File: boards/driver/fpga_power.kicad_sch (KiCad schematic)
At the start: 40 parts, among them J1 Barrel_Jack_Switch, J2 Conn_01x24, J3 Conn_02x06_Top_Bottom, J4 Conn_01x24, Q90 IRF7413, U10 74LVC245, U11 74LVC245, U12 JTE0624D05, U13 LTC4231-1, U14 74HC4514, U15 74LVC2G04, U16 74LVC2G04, U17 74LVC2G04, U18 74LVC2G04

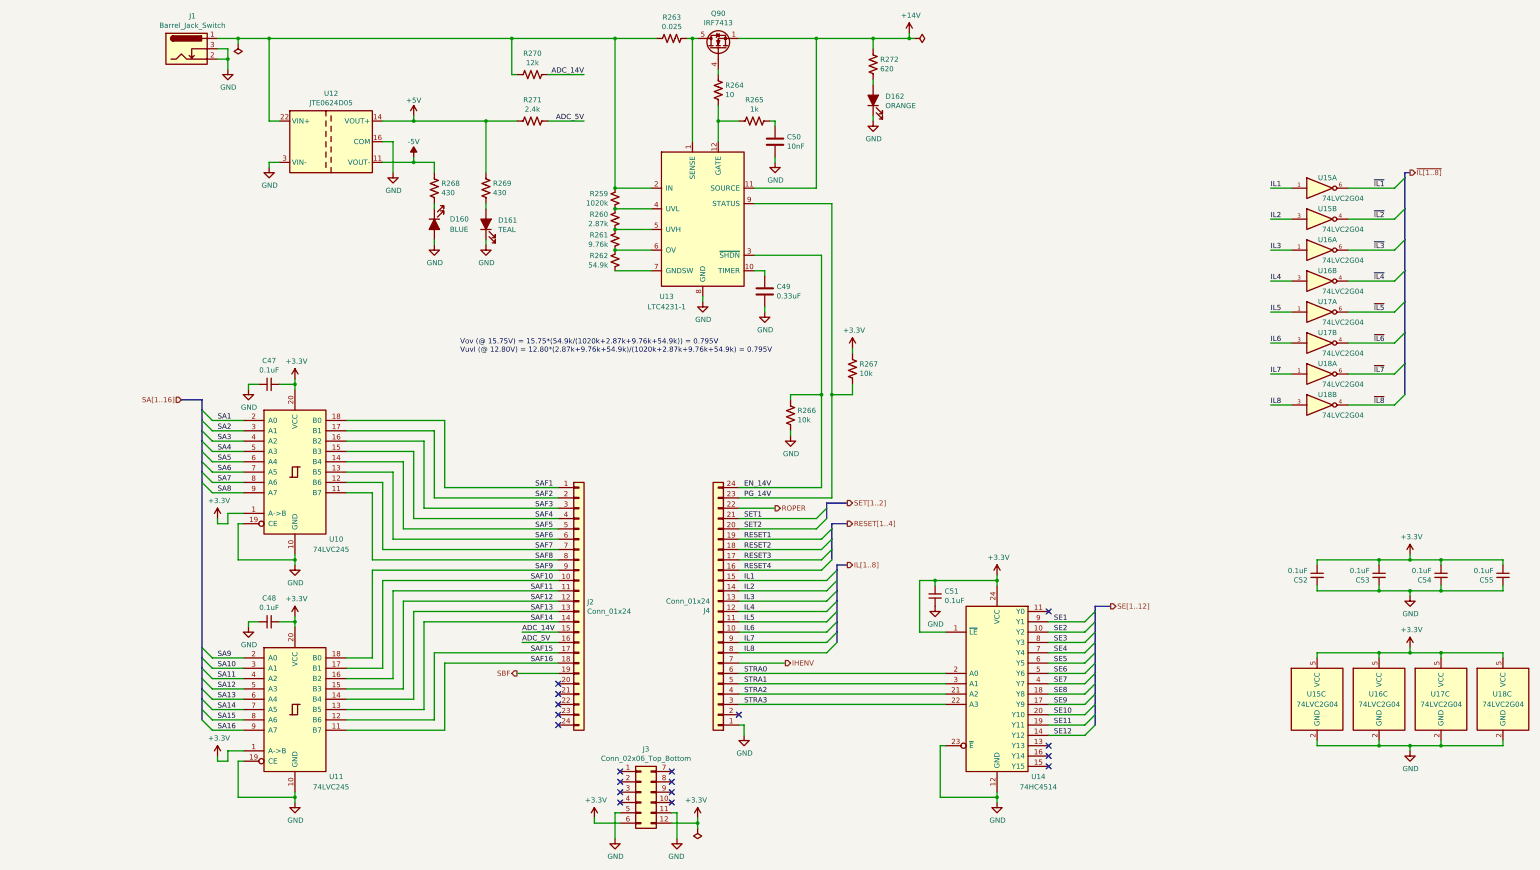
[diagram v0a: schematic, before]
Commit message: Driver: Added a 5V->3.3V LDO to replace the reversed cmod header, added jumpers for the 200R parallel returns, and renamed subcircuit ports to avoid unexpected ground connections.
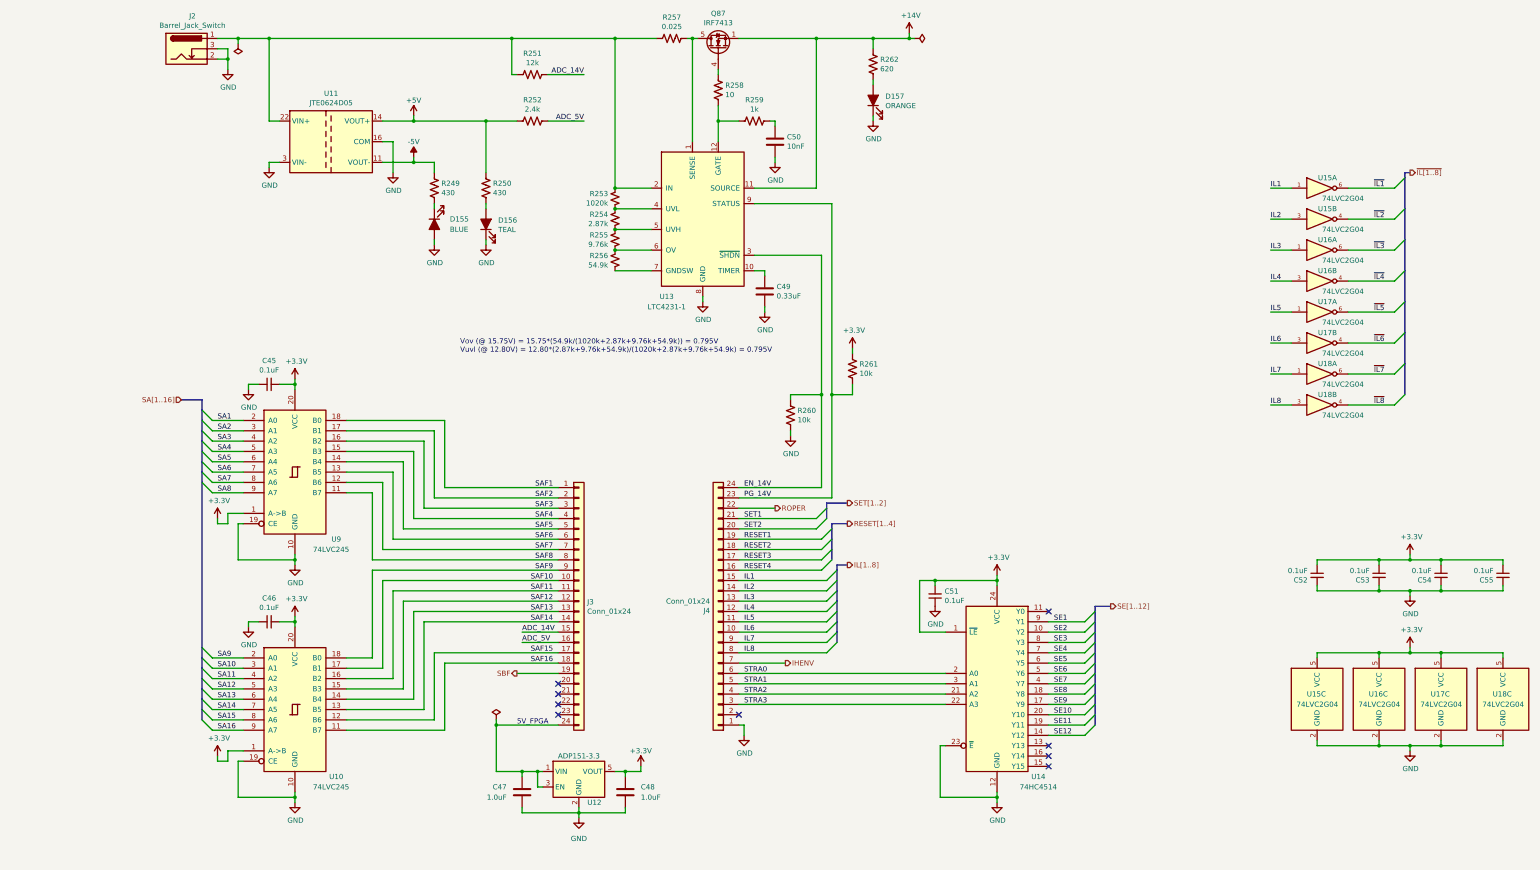
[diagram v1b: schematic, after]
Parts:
- removed J3: Conn_02x06_Top_Bottom, Connector_PinSocket_2.54mm:PinSocket_2x06_P2.54mm_Vertical, symbol Connector_Generic:Conn_02x06_Top_Bottom
- added C47, C48: 1.0uF, symbol Device:C
- added U12: ADP151-3.3, symbol lachesis:ADP151-3.3
- renumbered C47 to C45, C48 to C46, D160 to D155, D161 to D156, D162 to D157, J1 to J2, J2 to J3, Q90 to Q87, R268 to R249, R269 to R250, R270 to R251, R271 to R252, R259 to R253, R260 to R254, R261 to R255, R262 to R256, R263 to R257, R264 to R258, R265 to R259, R266 to R260, R267 to R261, R272 to R262, U11 to U10, U12 to U11, U10 to U9
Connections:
- net +3V3: now also C48.1, U12.5 (VOUT)
- net GND: now also C47.1, C48.2, U12.2 (GND)
- net at J3.24 (Pin_24): now also C47.2, U12.1 (VIN), U12.3 (EN)
- no-connect marks 18 -> 9
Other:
- note added: "5V_FPGA"

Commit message: Driver: incorporated most changes from the test board, and began layout
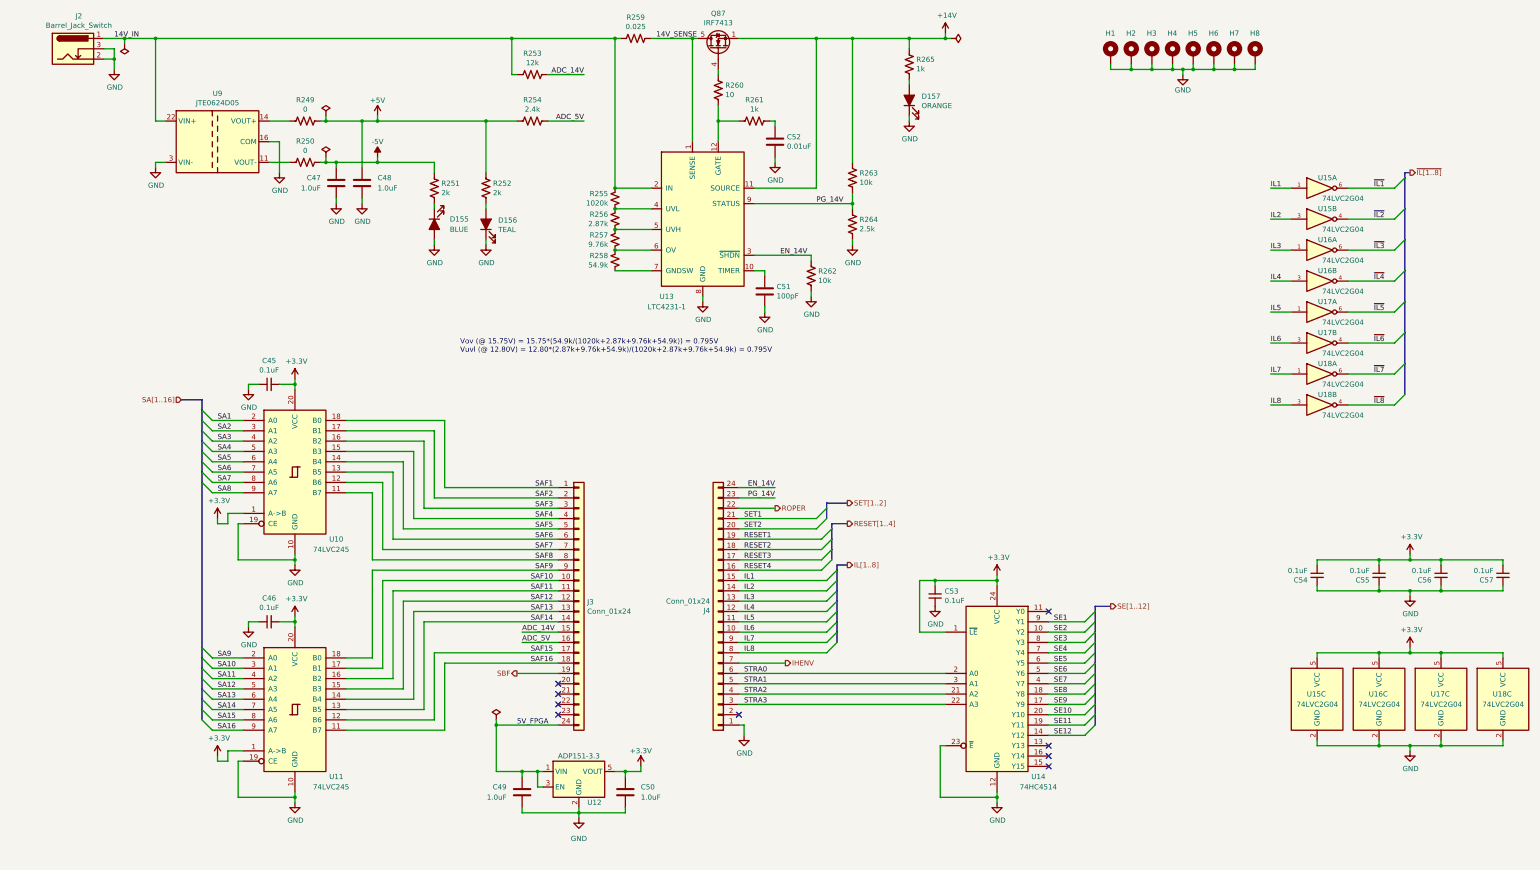
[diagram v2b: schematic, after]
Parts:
- added C47, C48: 1.0uF, Capacitor_SMD:C_0805_2012Metric, symbol Device:C
- added H1, H2, H3, H4, H5, H6, H7, H8: MountingHole_Pad, lachesis:MountingHole_No2_Pad, symbol Mechanical:MountingHole_Pad
- added R249, R250: 0, Resistor_SMD:R_0805_2012Metric, symbol Device:R_US
- added R264: 2.5k, Resistor_SMD:R_0603_1608Metric, symbol Device:R_US
- C49: renamed from C47; footprint (none) -> Capacitor_SMD:C_0603_1608Metric
- C50: renamed from C48; footprint (none) -> Capacitor_SMD:C_0603_1608Metric
- C51: renamed from C49; value 0.33uF -> 100pF
- C52: renamed from C50; value 10nF -> 0.01uF
- R251: renamed from R249; value 430 -> 2k
- R252: renamed from R250; value 430 -> 2k
- R259: renamed from R257; footprint Resistor_SMD:R_0603_1608Metric -> Resistor_SMD:R_1206_3216Metric
- R265: renamed from R262; value 620 -> 1k
- U12: footprint (none) -> Package_TO_SOT_SMD:TSOT-23-5
- renumbered C51 to C53, C52 to C54, C53 to C55, C54 to C56, C55 to C57, R251 to R253, R252 to R254, R253 to R255, R254 to R256, R255 to R257, R256 to R258, R258 to R260, R259 to R261, R260 to R262, R261 to R263, U9 to U10, U10 to U11, U11 to U9
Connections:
- net +14V: now also R263.1
- net +3V3: no longer R263.1
- net +5V: now also C48.1, R249.1; no longer U9.14 (VOUT+)
- net -5V: now also C47.2, R250.1; no longer U9.11 (VOUT-)
- net GND: now also C47.1, C48.2, H1.1, H2.1, H3.1, H4.1, H5.1, H6.1, H7.1, H8.1, R264.2
- net PG_14V: now also R264.1
- net 14V_SENSE: now reaches Q87.5 (D), Q87.6 (D), Q87.7 (D), Q87.8 (D), R259.1, U13.1 (SENSE)
- net 14V_IN: now reaches J2.1, R253.2, R255.2, R259.2, U13.2 (IN), U9.22 (VIN+), U9.23 (VIN+)
- new net: R250.2, U9.11 (VOUT-)
- new net: R249.2, U9.14 (VOUT+)
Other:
- moved on the sheet: D157, J2, R259, R262, R263, R265, U9

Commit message: Driver: lightly reorganized FPGA wiring to make it easier to change in the future, and fixed sense amp mapping
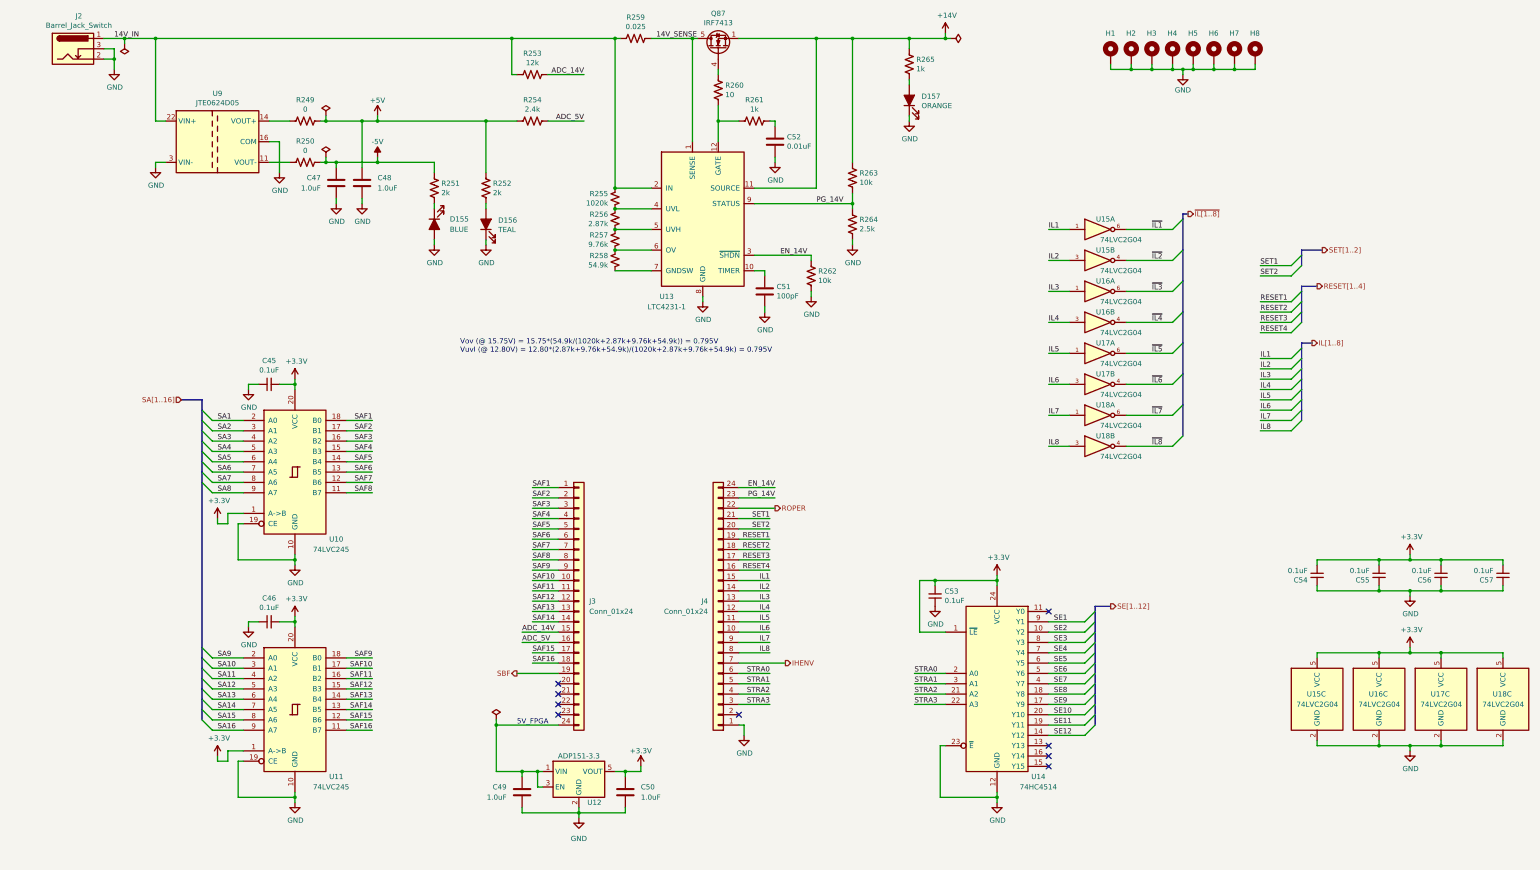
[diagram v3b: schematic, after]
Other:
- moved on the sheet: U15A, U15B, U16A, U16B, U17A, U17B, U18A, U18B

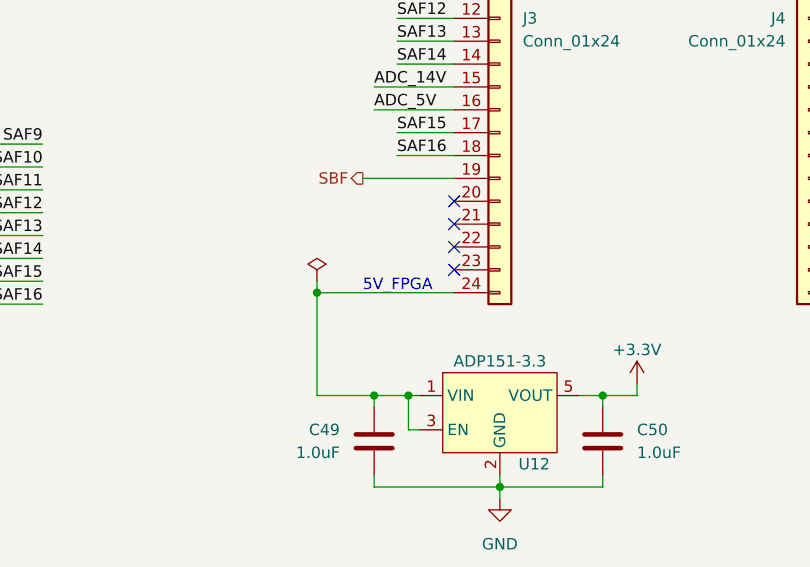
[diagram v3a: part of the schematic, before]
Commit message: Driver: progress on subcircuit layout and overall placement
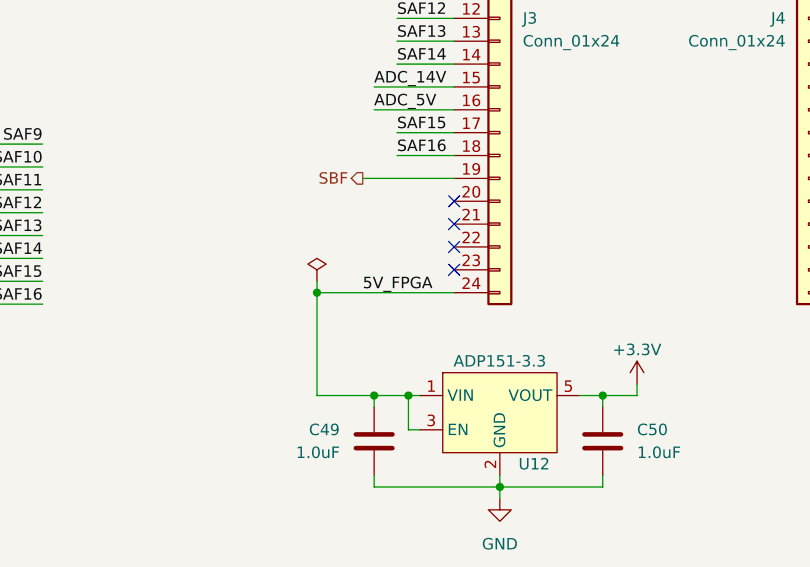
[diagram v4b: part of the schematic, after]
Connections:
- net 5V_FPGA: now reaches C49.2, J3.24 (Pin_24), U12.1 (VIN), U12.3 (EN)
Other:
- note removed: "5V_FPGA"
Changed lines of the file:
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@@
-    (effects (font (size 1.27 1.27)) (justify left bottom))
-  )
-  (text "5V_FPGA" (at 142.24 205.74 0)
     (effects (font (size 1.27 1.27)) (justify left bottom))
   )
@@
     (effects (font (size 1.27 1.27)) (justify left bottom))
   )
+  (label "5V_FPGA" (at 142.24 205.74 0)
+    (effects (font (size 1.27 1.27)) (justify left bottom))
+  )

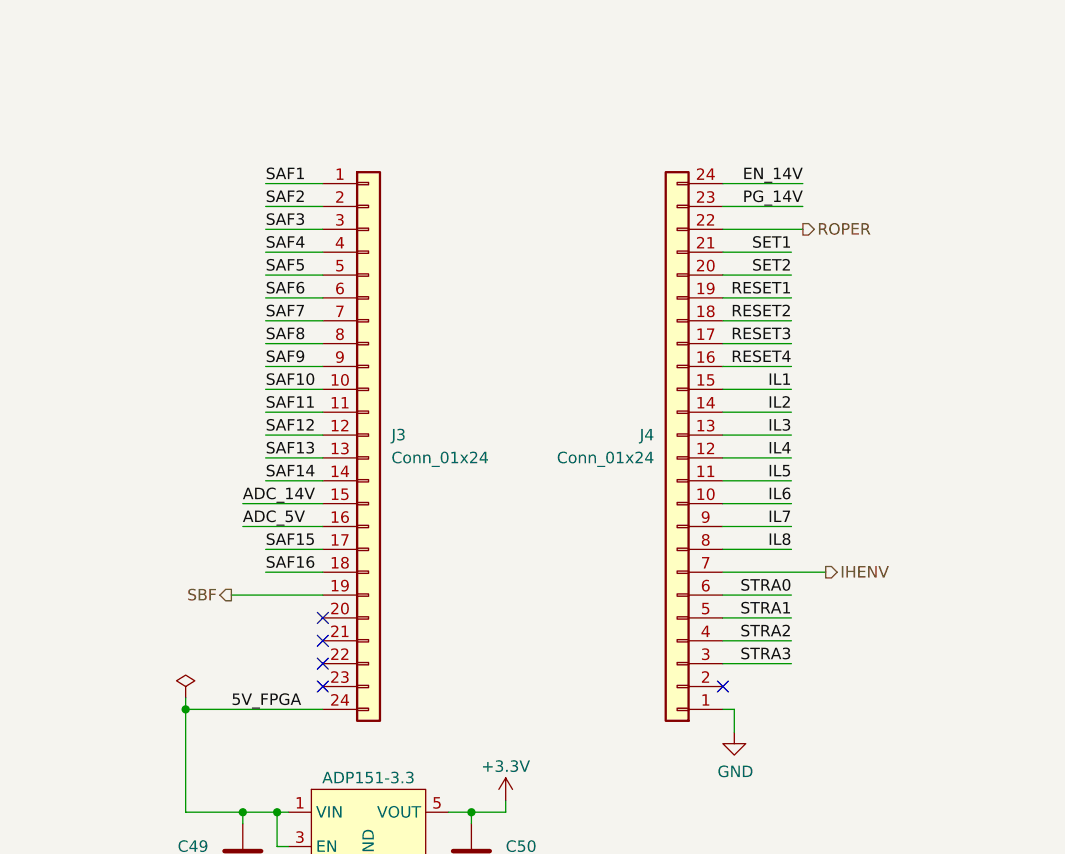
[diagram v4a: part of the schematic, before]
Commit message: Driver: 3.3V section is now laid out, contained entirely beneath the FPGA daughter board
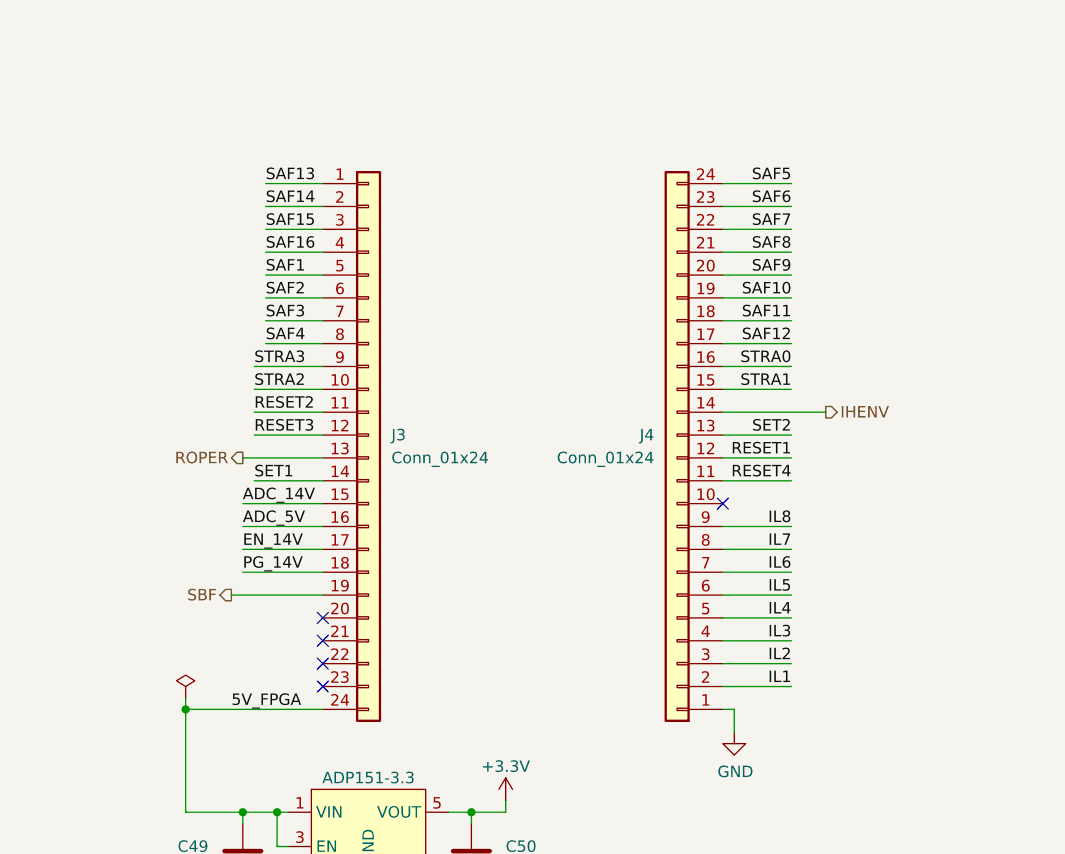
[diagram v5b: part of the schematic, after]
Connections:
- net EN_14V: now also J3.17 (Pin_17); no longer J4.24 (Pin_24)
- net IHENV: now also J4.14 (Pin_14); no longer J4.7 (Pin_7)
- net IL1: now also J4.2 (Pin_2); no longer J4.15 (Pin_15)
- net IL2: now also J4.3 (Pin_3); no longer J4.14 (Pin_14)
- net IL3: now also J4.4 (Pin_4); no longer J4.13 (Pin_13)
- net IL4: now also J4.5 (Pin_5); no longer J4.12 (Pin_12)
- net IL5: now also J4.6 (Pin_6); no longer J4.11 (Pin_11)
- net IL6: now also J4.7 (Pin_7); no longer J4.10 (Pin_10)
- net IL7: now also J4.8 (Pin_8); no longer J4.9 (Pin_9)
- net IL8: now also J4.9 (Pin_9); no longer J4.8 (Pin_8)
- net PG_14V: now also J3.18 (Pin_18); no longer J4.23 (Pin_23)
- net RESET1: now also J4.12 (Pin_12); no longer J4.19 (Pin_19)
- net RESET2: now also J3.11 (Pin_11); no longer J4.18 (Pin_18)
- net RESET3: now also J3.12 (Pin_12); no longer J4.17 (Pin_17)
- net RESET4: now also J4.11 (Pin_11); no longer J4.16 (Pin_16)
- net ROPER: now also J3.13 (Pin_13); no longer J4.22 (Pin_22)
- net SAF1: now also J3.5 (Pin_5); no longer J3.1 (Pin_1)
- net SAF10: now also J4.19 (Pin_19); no longer J3.10 (Pin_10)
- net SAF11: now also J4.18 (Pin_18); no longer J3.11 (Pin_11)
- net SAF12: now also J4.17 (Pin_17); no longer J3.12 (Pin_12)
- net SAF13: now also J3.1 (Pin_1); no longer J3.13 (Pin_13)
- net SAF14: now also J3.2 (Pin_2); no longer J3.14 (Pin_14)
- net SAF15: now also J3.3 (Pin_3); no longer J3.17 (Pin_17)
- net SAF16: now also J3.4 (Pin_4); no longer J3.18 (Pin_18)
- net SAF2: now also J3.6 (Pin_6); no longer J3.2 (Pin_2)
- net SAF3: now also J3.7 (Pin_7); no longer J3.3 (Pin_3)
- net SAF4: now also J3.8 (Pin_8); no longer J3.4 (Pin_4)
- net SAF5: now also J4.24 (Pin_24); no longer J3.5 (Pin_5)
- net SAF6: now also J4.23 (Pin_23); no longer J3.6 (Pin_6)
- net SAF7: now also J4.22 (Pin_22); no longer J3.7 (Pin_7)
- net SAF8: now also J4.21 (Pin_21); no longer J3.8 (Pin_8)
- net SAF9: now also J4.20 (Pin_20); no longer J3.9 (Pin_9)
- net SET1: now also J3.14 (Pin_14); no longer J4.21 (Pin_21)
- net SET2: now also J4.13 (Pin_13); no longer J4.20 (Pin_20)
- net STRA0: now also J4.16 (Pin_16); no longer J4.6 (Pin_6)
- net STRA1: now also J4.15 (Pin_15); no longer J4.5 (Pin_5)
- net STRA2: now also J3.10 (Pin_10); no longer J4.4 (Pin_4)
- net STRA3: now also J3.9 (Pin_9); no longer J4.3 (Pin_3)
